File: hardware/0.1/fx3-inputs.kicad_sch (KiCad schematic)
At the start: 1 part, among them U301 CYUSB3014-BZXx

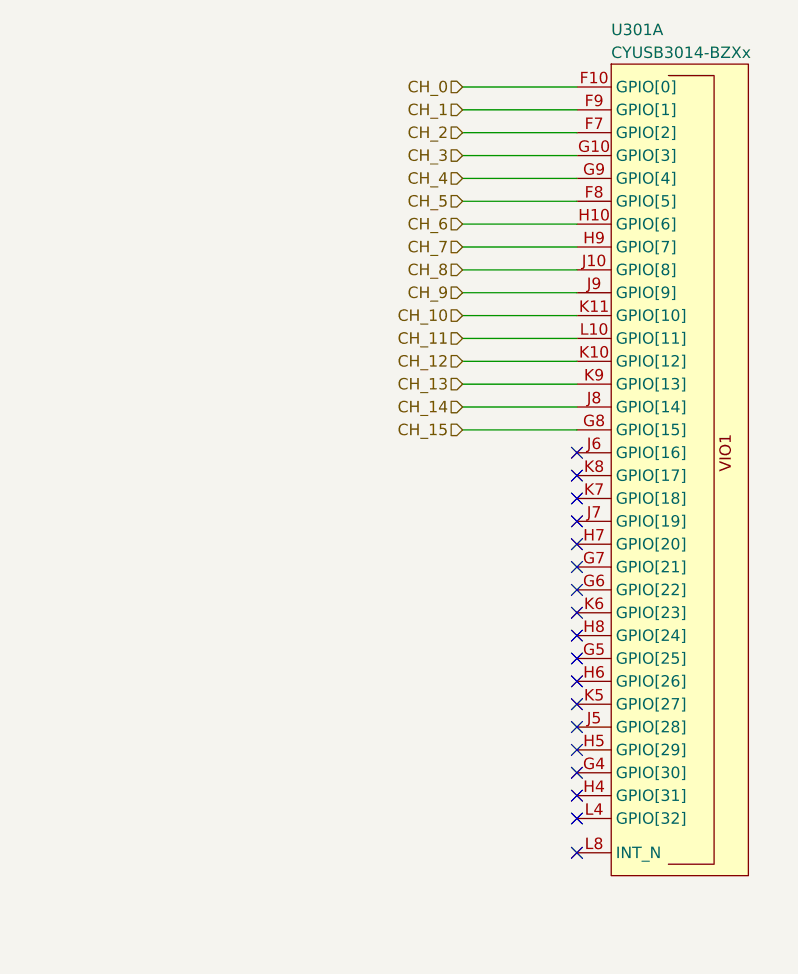
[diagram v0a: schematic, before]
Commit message: break out bga
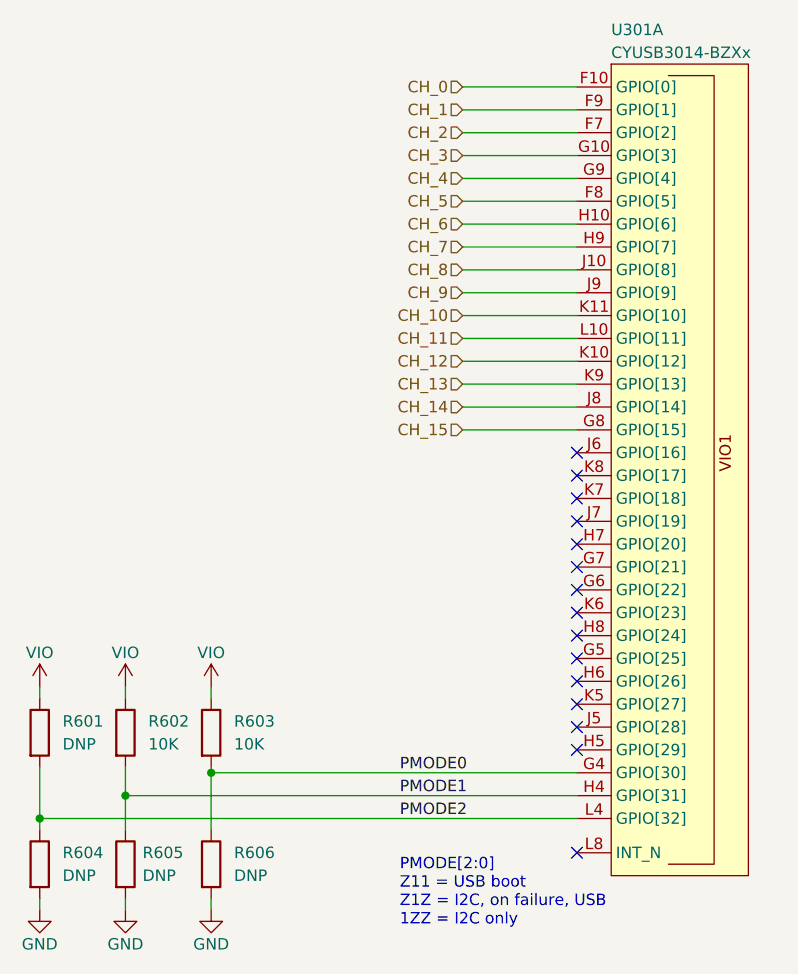
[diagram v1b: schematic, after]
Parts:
- added R601, R604, R605, R606: DNP, Resistor_SMD:R_0402_1005Metric, symbol Device:R
- added R602, R603: 10K, Resistor_SMD:R_0402_1005Metric, symbol Device:R
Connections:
- net PMODE0: now reaches U301.G4 (GPIO[30])
- net PMODE0: now also R603.2, R606.1
- net PMODE1: now reaches U301.H4 (GPIO[31])
- net PMODE1: now also R602.2, R605.1
- net PMODE2: now reaches U301.L4 (GPIO[32])
- net PMODE2: now also R601.2, R604.1
- new net GND: R604.2, R605.2, R606.2
- new net VIO: R601.1, R602.1, R603.1
- no-connect marks 18 -> 15
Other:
- note added: "PMODE[2:0] Z11 = USB boot Z1Z = I2C, on failure, USB 1ZZ = I2C only"

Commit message: erc = drc = 0, fixup BOM
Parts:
- R602, R603: LCSC (none) -> C60490; MPN (none) -> RC0402FR-0710KL; Manufacturer (none) -> Yageo
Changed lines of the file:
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@@
+      (effects (font (size 1.27 1.27)) hide)
+    )
+    (property "LCSC" "C60490" (id 4) (at 86.36 132.08 0)
+      (effects (font (size 1.27 1.27)) hide)
+    )
+    (property "MPN" "RC0402FR-0710KL" (id 5) (at 86.36 132.08 0)
+      (effects (font (size 1.27 1.27)) hide)
+    )
+    (property "Manufacturer" "Yageo" (id 6) (at 86.36 132.08 0)
       (effects (font (size 1.27 1.27)) hide)
     )
@@
       (effects (font (size 1.27 1.27)) hide)
     )
+    (property "LCSC" "C60490" (id 4) (at 76.835 132.08 0)
+      (effects (font (size 1.27 1.27)) hide)
+    )
+    (property "MPN" "RC0402FR-0710KL" (id 5) (at 76.835 132.08 0)
+      (effects (font (size 1.27 1.27)) hide)
+    )
+    (property "Manufacturer" "Yageo" (id 6) (at 76.835 132.08 0)
+      (effects (font (size 1.27 1.27)) hide)
+    )
